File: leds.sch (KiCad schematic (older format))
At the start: 55 parts, among them U1 TLC5955, U2 TLC5955, U3 TLC5955

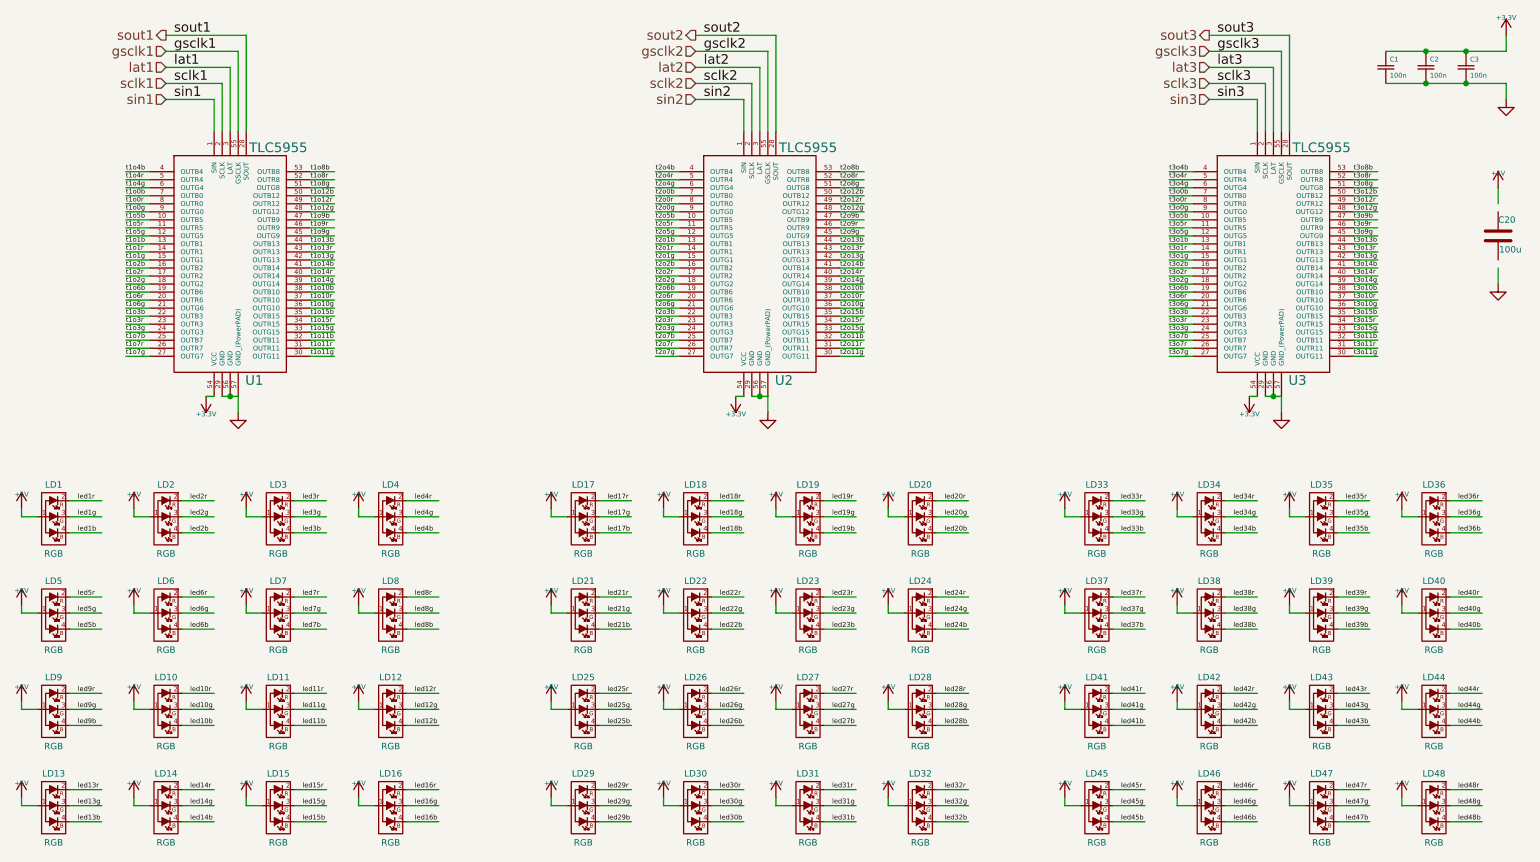
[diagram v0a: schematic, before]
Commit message: Assignment of LEDs to TLC5955 outputs.
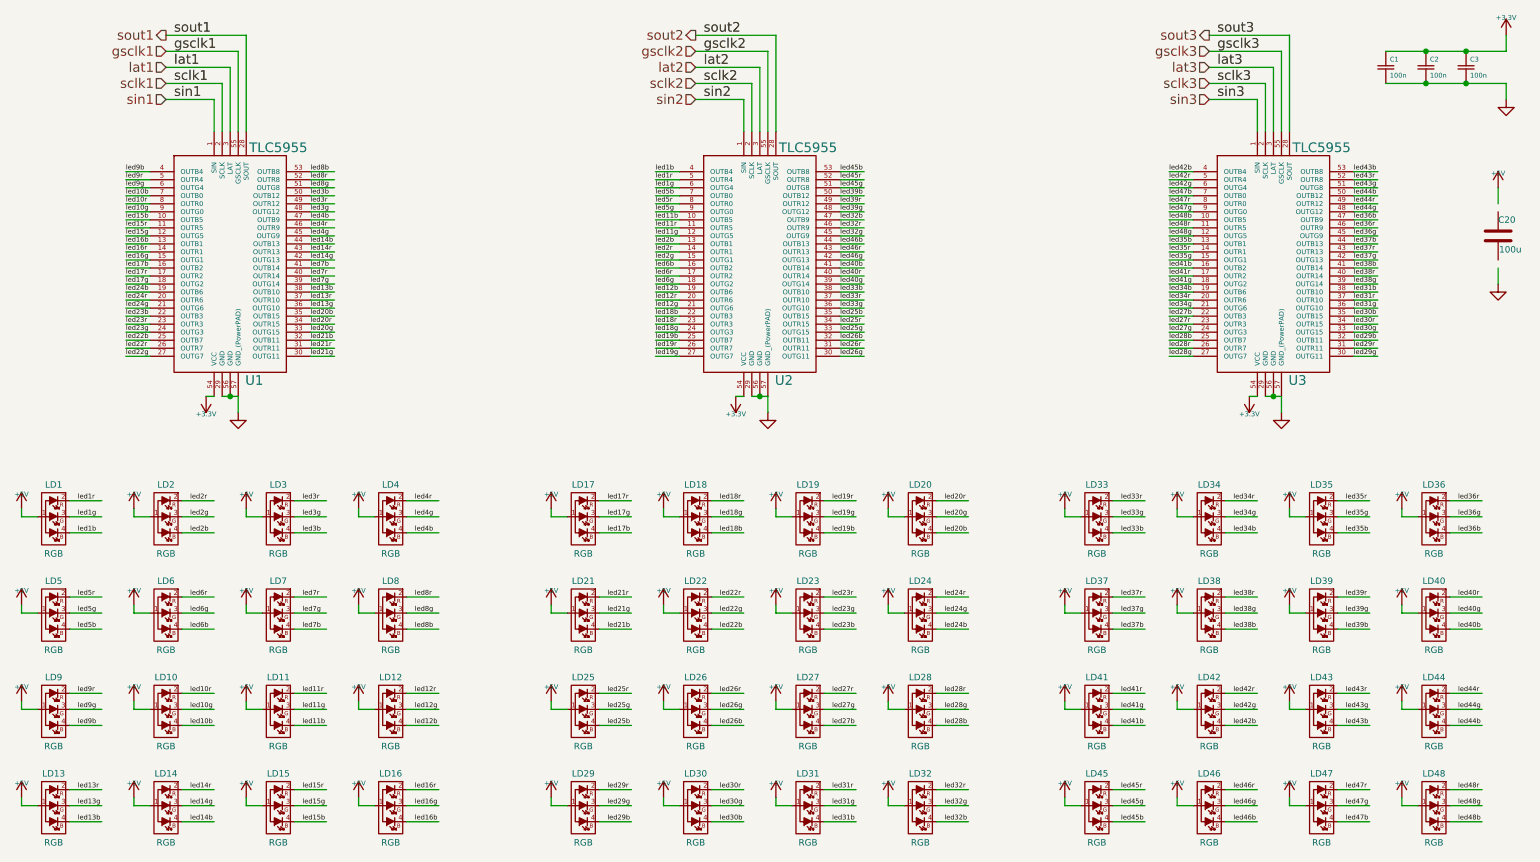
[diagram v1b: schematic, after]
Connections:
- net labels removed: t1o0b, t1o0g, t1o0r, t1o10b, t1o10g, t1o10r, t1o11b, t1o11g, t1o11r, t1o12b, t1o12g, t1o12r, t1o13b, t1o13g, t1o13r, t1o14b, t1o14g, t1o14r, t1o15b, t1o15g, t1o15r, t1o1b, t1o1g, t1o1r, t1o2b, t1o2g, t1o2r, t1o3b, t1o3g, t1o3r, t1o4b, t1o4g, t1o4r, t1o5b, t1o5g, t1o5r, t1o6b, t1o6g, t1o6r, t1o7b, t1o7g, t1o7r, t1o8b, t1o8g, t1o8r, t1o9b, t1o9g, t1o9r, t2o0b, t2o0g, t2o0r, t2o10b, t2o10g, t2o10r, t2o11b, t2o11g, t2o11r, t2o12b, t2o12g, t2o12r, t2o13b, t2o13g, t2o13r, t2o14b, t2o14g, t2o14r, t2o15b, t2o15g, t2o15r, t2o1b, t2o1g, t2o1r, t2o2b, t2o2g, t2o2r, t2o3b, t2o3g, t2o3r, t2o4b, t2o4g, t2o4r, t2o5b, t2o5g, t2o5r, t2o6b, t2o6g, t2o6r, t2o7b, t2o7g, t2o7r, t2o8b, t2o8g, t2o8r, t2o9b, t2o9g, t2o9r, t3o0b, t3o0g, t3o0r, t3o10b, t3o10g, t3o10r, t3o11b, t3o11g, t3o11r, t3o12b, t3o12g, t3o12r, t3o13b, t3o13g, t3o13r, t3o14b, t3o14g, t3o14r, t3o15b, t3o15g, t3o15r, t3o1b, t3o1g, t3o1r, t3o2b, t3o2g, t3o2r, t3o3b, t3o3g, t3o3r, t3o4b, t3o4g, t3o4r, t3o5b, t3o5g, t3o5r, t3o6b, t3o6g, t3o6r, t3o7b, t3o7g, t3o7r, t3o8b, t3o8g, t3o8r, t3o9b, t3o9g, t3o9r

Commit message: LED routing, and initial placement of most remaining components.
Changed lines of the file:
@@
 led44g
 Text Label 9500 2350 0    30   ~ 0
+led37b
+Text Label 9500 2400 0    30   ~ 0
+led37r
+Text Label 9500 2450 0    30   ~ 0
+led37g
+Text Label 9500 2500 0    30   ~ 0
 led36b
-Text Label 9500 2400 0    30   ~ 0
+Text Label 9500 2550 0    30   ~ 0
 led36r
-Text Label 9500 2450 0    30   ~ 0
+Text Label 9500 2600 0    30   ~ 0
 led36g
-Text Label 9500 2500 0    30   ~ 0
-led37b
-Text Label 9500 2550 0    30   ~ 0
-led37r
-Text Label 9500 2600 0    30   ~ 0
-led37g
 Text Label 9500 2650 0    30   ~ 0
 led38b

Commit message: Complete routing
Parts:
- C1, C2, C3: footprint (none) -> w_smd_cap:c_0805
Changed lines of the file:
@@
 F 0 "C1" H 9725 1450 30  0000 L CNN
 F 1 "100n" H 9725 1350 30  0000 L CNN
-F 2 "" H 9700 1400 60  0000 C CNN
+F 2 "w_smd_cap:c_0805" H 9700 1400 60  0001 C CNN
 F 3 "" H 9700 1400 60  0000 C CNN
 	1    9700 1400
@@
 F 0 "C2" H 9975 1450 30  0000 L CNN
 F 1 "100n" H 9975 1350 30  0000 L CNN
-F 2 "" H 9950 1400 60  0000 C CNN
+F 2 "w_smd_cap:c_0805" H 9950 1400 60  0001 C CNN
 F 3 "" H 9950 1400 60  0000 C CNN
 	1    9950 1400
@@
 F 0 "C3" H 10225 1450 30  0000 L CNN
 F 1 "100n" H 10225 1350 30  0000 L CNN
-F 2 "" H 10200 1400 60  0000 C CNN
+F 2 "w_smd_cap:c_0805" H 10200 1400 60  0001 C CNN
 F 3 "" H 10200 1400 60  0000 C CNN
 	1    10200 1400

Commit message: Fixup some missing wires after kicad upgrade
(A resistor and a capacitor component now has shorter leads, it seems.
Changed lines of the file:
@@
 	9650 3200 9500 3200
 Wire Wire Line
-	10400 2650 10400 2750
+	10400 2600 10400 2750
 Wire Wire Line
-	10400 2250 10400 2150
+	10400 2300 10400 2150
 Wire Wire Line
 	2400 3450 2350 3450

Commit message: Move 2 TLCs 4mm to not conflict with spindle mount rim
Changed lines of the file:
@@
 led44g
 Text Label 9500 2350 0    30   ~ 0
+led36b
+Text Label 9500 2400 0    30   ~ 0
+led36r
+Text Label 9500 2450 0    30   ~ 0
+led36g
+Text Label 9500 2500 0    30   ~ 0
 led37b
-Text Label 9500 2400 0    30   ~ 0
+Text Label 9500 2550 0    30   ~ 0
 led37r
-Text Label 9500 2450 0    30   ~ 0
+Text Label 9500 2600 0    30   ~ 0
 led37g
-Text Label 9500 2500 0    30   ~ 0
-led36b
-Text Label 9500 2550 0    30   ~ 0
-led36r
-Text Label 9500 2600 0    30   ~ 0
-led36g
 Text Label 9500 2650 0    30   ~ 0
 led38b
